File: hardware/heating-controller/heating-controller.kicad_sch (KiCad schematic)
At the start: 22 parts, among them J1 LilyGo T-Display S3, J2 Temperature_probes, J3 Power connector, K1 FINDER-32.21-x000, Q1 AO3400A, U1 H11AA1

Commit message: First PCB, needs to be checked
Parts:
- added R1, R5: 15k, Resistor_SMD:R_0603_1608Metric, symbol Device:R
- C1: renamed from C2; footprint Resistor_SMD:R_0201_0603Metric -> Capacitor_SMD:C_0603_1608Metric
- renumbered C3 to C2, C1 to C3, F2 to F1, F1 to F2, R3 to R2, R2 to R3, R1 to R4, R4 to R6, R5 to R7, R6 to R8, RV2 to RV1, RV1 to RV2
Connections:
- net EXT_TEMP_1 is gone; now on net EXT_TEMP: J2.1 (Pin_1)
- net LIM_TEMP_1 is gone; now on net LIMITER_TEMP: J2.3 (Pin_3)
- net +3.3V: now also R1.1, R5.1
- net EXT_TEMP: now also R1.2
- net LIMITER_TEMP: now also R5.2
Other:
- note added: "NTC acquisition"
- moved on the sheet: C1, C2, C3, D1, D2, F1, F2, K1, PS1, Q1, R2, R3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

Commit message: WIP
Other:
- note added: "(ADC1_CH0) 1"
- note added: "(ADC1_CH1) 2"
- note added: "(GPIO 10) 10"
- note added: "(GPIO 11) 11"
- note added: "(GPIO 12) 12"
- note added: "(GPIO 13) 13"
- note added: "(GPIO 3) 3"
- note added: "3V"
- note added: "5V"
- note added: "GND"
- note added: "NC"
- moved on the sheet: C1, C2, C3, D1, D2, F1, F2, J1, J2, J3, K1, PS1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

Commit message: WIP
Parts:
- added D1: 1N4148WS, Diode_SMD:D_SOD-323, symbol Diode:1N4148WS
- added D3: LED, LED_SMD:LED_0805_2012Metric, symbol Device:LED_Small
- added J4: EXT_LED, Connector_PinHeader_2.54mm:PinHeader_1x02_P2.54mm_Vertical, symbol Connector_Generic:Conn_01x02
- added R7, R9: 470, Resistor_SMD:R_0603_1608Metric, symbol Device:R
- C3: renamed from C2; footprint Capacitor_THT:C_Radial_D6.3mm_H7.0mm_P2.50mm -> Capacitor_THT:C_Radial_D10.0mm_H12.5mm_P5.00mm
- J1: renamed from J2; footprint Connector_Phoenix_MSTB:PhoenixContact_MSTBVA_2,5_4-G_1x04_P5.00mm_Vertical -> TerminalBlock_Phoenix:TerminalBlock_Phoenix_MKDS-3-4-5.08_1x04_P5.08mm_Horizontal
- J3: footprint Connector_Phoenix_MSTB:PhoenixContact_MSTBVA_2,5_7-G_1x07_P5.00mm_Vertical -> TerminalBlock_Phoenix:TerminalBlock_Phoenix_MKDS-3-7-5.08_1x07_P5.08mm_Horizontal
- R5: renamed from R2; footprint Resistor_THT:R_Axial_DIN0204_L3.6mm_D1.6mm_P5.08mm_Horizontal -> Resistor_THT:R_Axial_DIN0614_L14.3mm_D5.7mm_P15.24mm_Horizontal
- renumbered C3 to C1, C1 to C2, D1 to D2, D2 to D4, F2 to F1, F1 to F2, J1 to J2, R8 to R10, R3 to R2, R4 to R3, R5 to R4, R7 to R8, RV2 to RV1, RV1 to RV2
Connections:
- net +5V: now also D1.2 (A), R7.2, R9.2; no longer J2.12 (Pin_12)
- net at D4.2 (A), K1.A2, Q1.3 (D): now also D3.1 (K), J4.1 (Pin_1)
- new net: D3.2 (A), R9.1
- new net: J4.2 (Pin_2), R7.1
- new net: D1.1 (K), J2.12 (Pin_12)
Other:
- moved on the sheet: D4

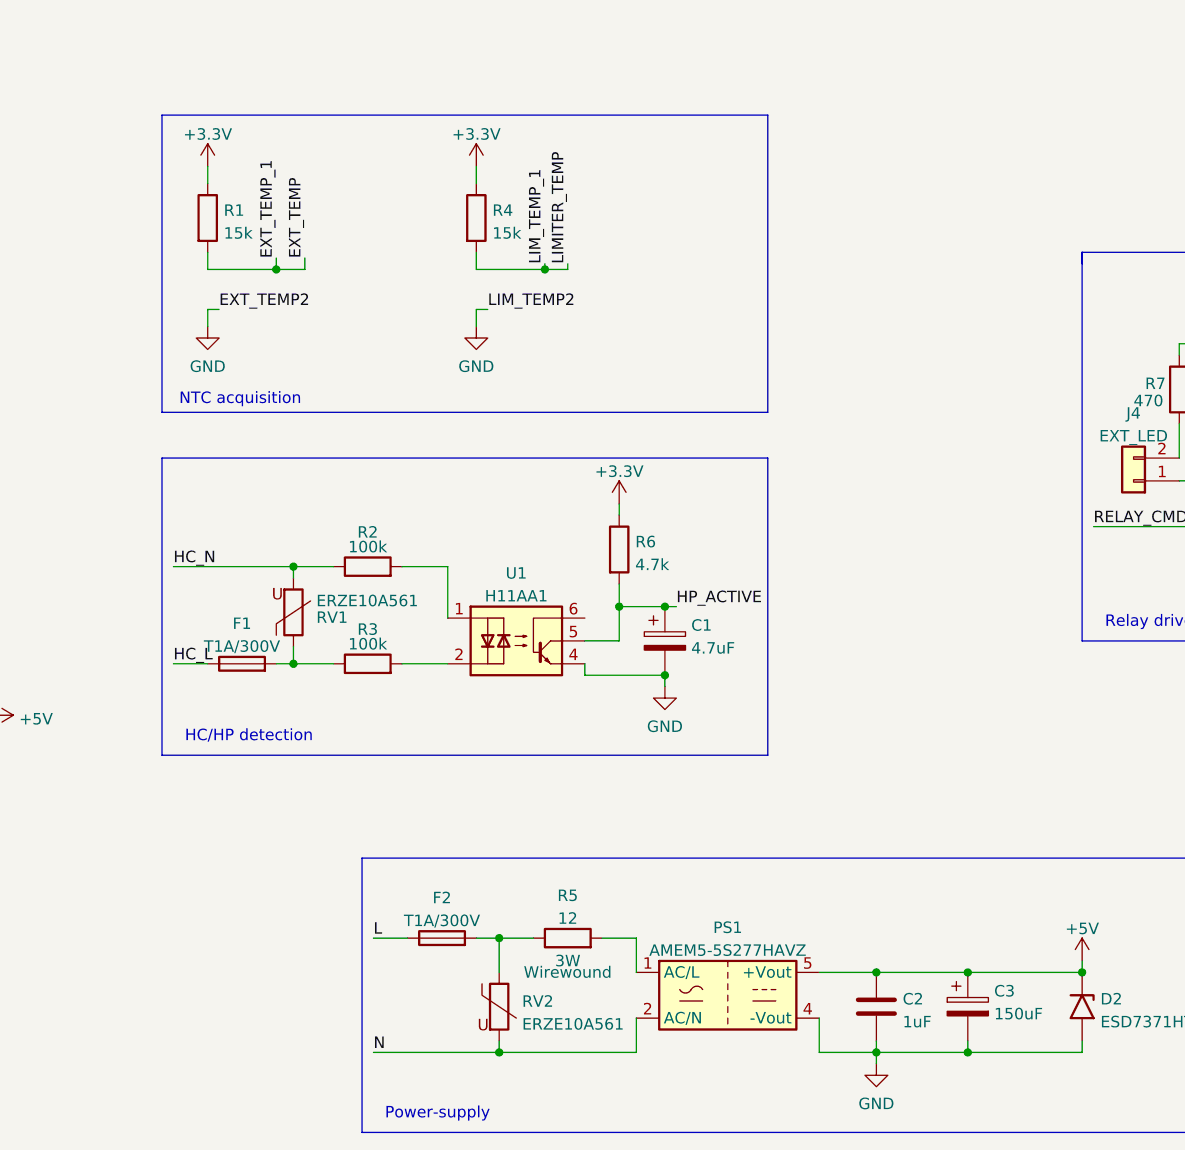
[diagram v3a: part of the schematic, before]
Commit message: Added 10uF capacitors to NTC
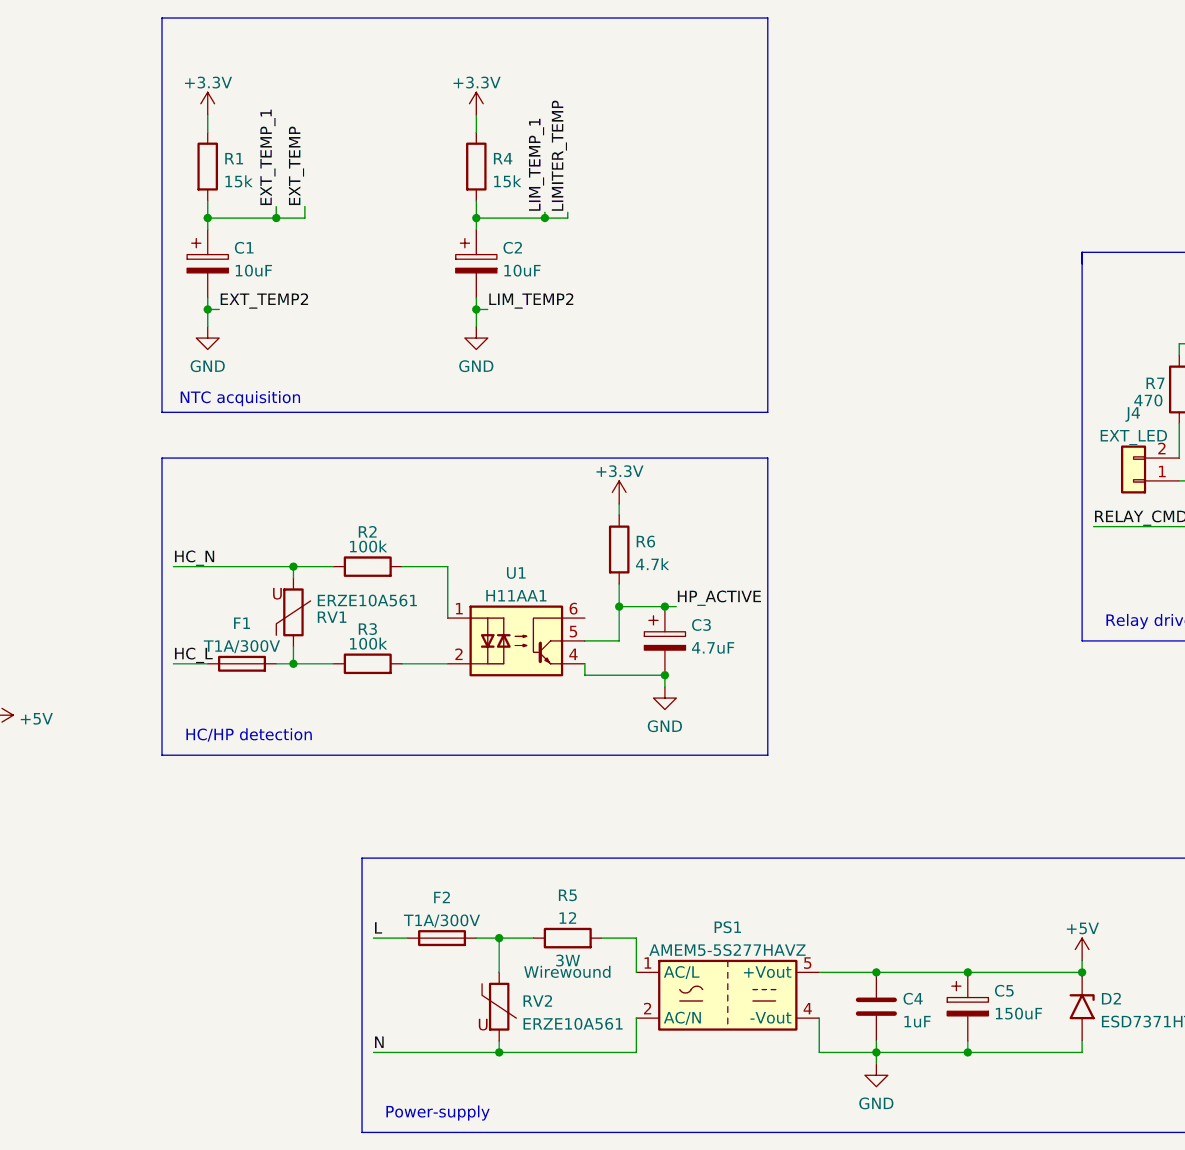
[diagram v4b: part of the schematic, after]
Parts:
- added C1, C2: 10uF, Capacitor_SMD:C_0805_2012Metric, symbol Device:C_Polarized
- renumbered C1 to C3, C2 to C4, C3 to C5
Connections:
- net EXT_TEMP: now also C1.1
- net GND: now also C1.2, C2.2
- net LIMITER_TEMP: now also C2.1
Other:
- moved on the sheet: R1, R4

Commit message: WIP
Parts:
- added J5: USER_LED, Connector_PinHeader_2.54mm:PinHeader_1x02_P2.54mm_Vertical, symbol Connector_Generic:Conn_01x02
- added Q1: AO3400A, Package_TO_SOT_SMD:SOT-23, symbol Transistor_FET:AO3400A
- added R11: 100k, Resistor_SMD:R_0603_1608Metric, symbol Device:R
- added R13: 470, Resistor_SMD:R_0603_1608Metric, symbol Device:R
- added R8: 1k, Resistor_SMD:R_0603_1608Metric, symbol Device:R
- R10: renamed from R9; value 470 -> 2k
- renumbered D3 to D2, D2 to D3, Q1 to Q2, R10 to R12, R8 to R9
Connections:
- net EXT_TEMP_2 is gone; now on net GND: J1.2 (Pin_2)
- net LIM_TEMP_2 is gone; now on net GND: J1.4 (Pin_4)
- net +5V: now also R13.2
- net GND: now also Q1.2 (S), R11.2
- net USER_LED: now reaches J2.6 (Pin_6)
- net USER_LED: now also R8.1
- new net: Q1.1 (G), R11.1, R8.2
- new net: J5.1 (Pin_1), Q1.3 (D)
- new net: J5.2 (Pin_2), R13.1
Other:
- note added: "User LED"
- moved on the sheet: D2, D4, J4, K1, Q2, R10, R12, R7, R9

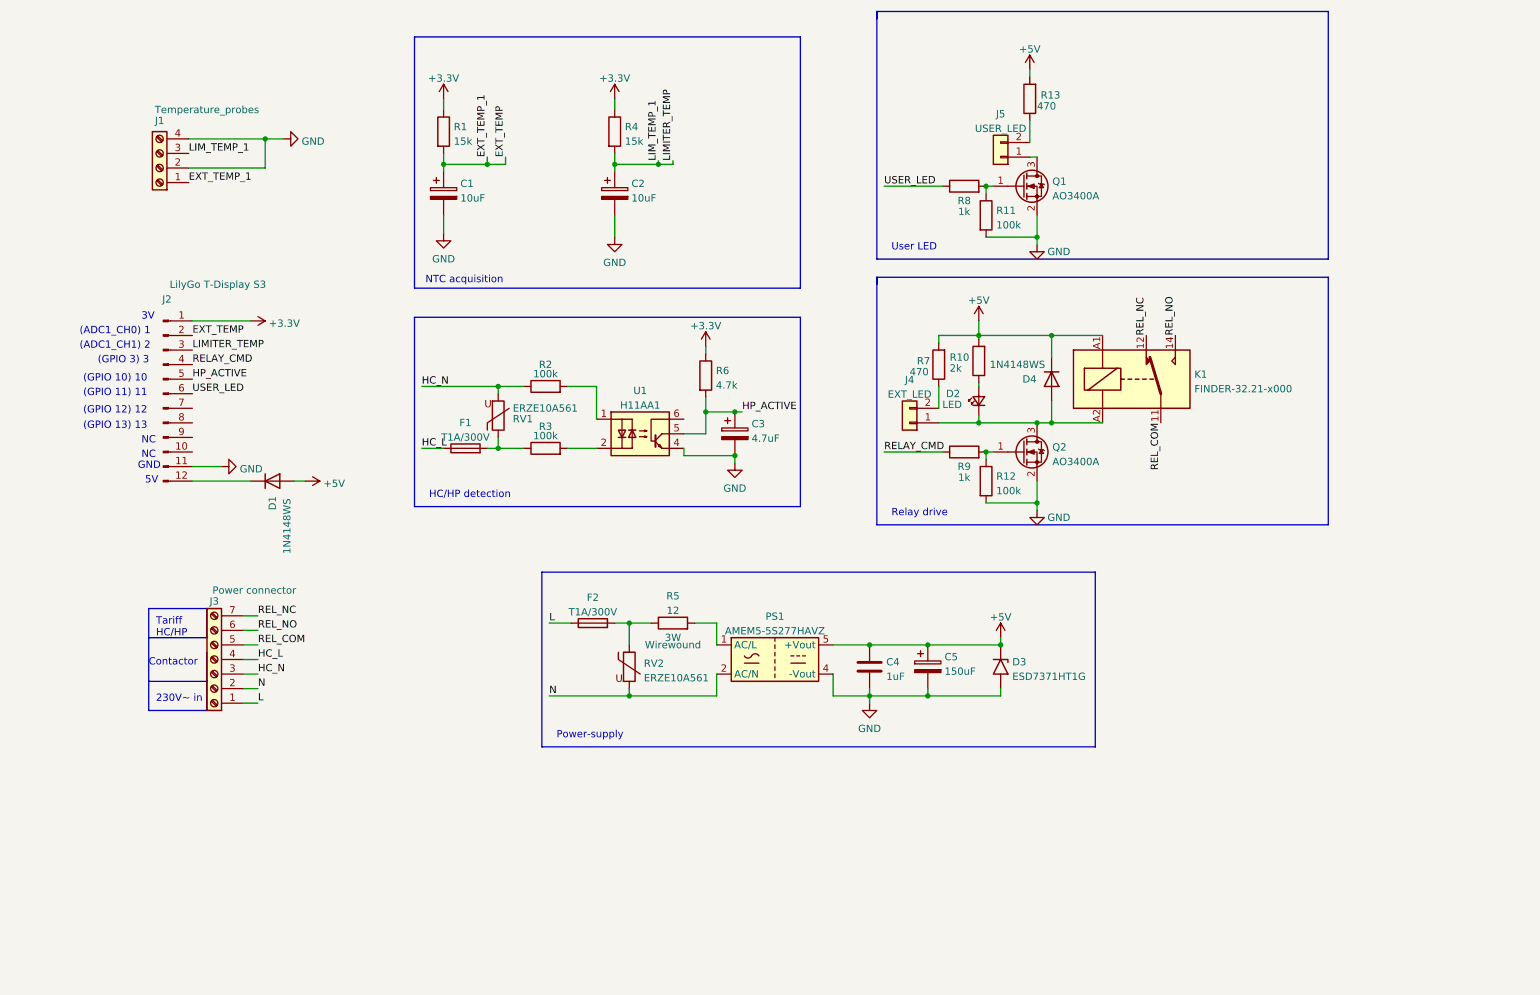
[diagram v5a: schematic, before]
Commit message: Migrated to KiCad 7 and remove custom AC/DC
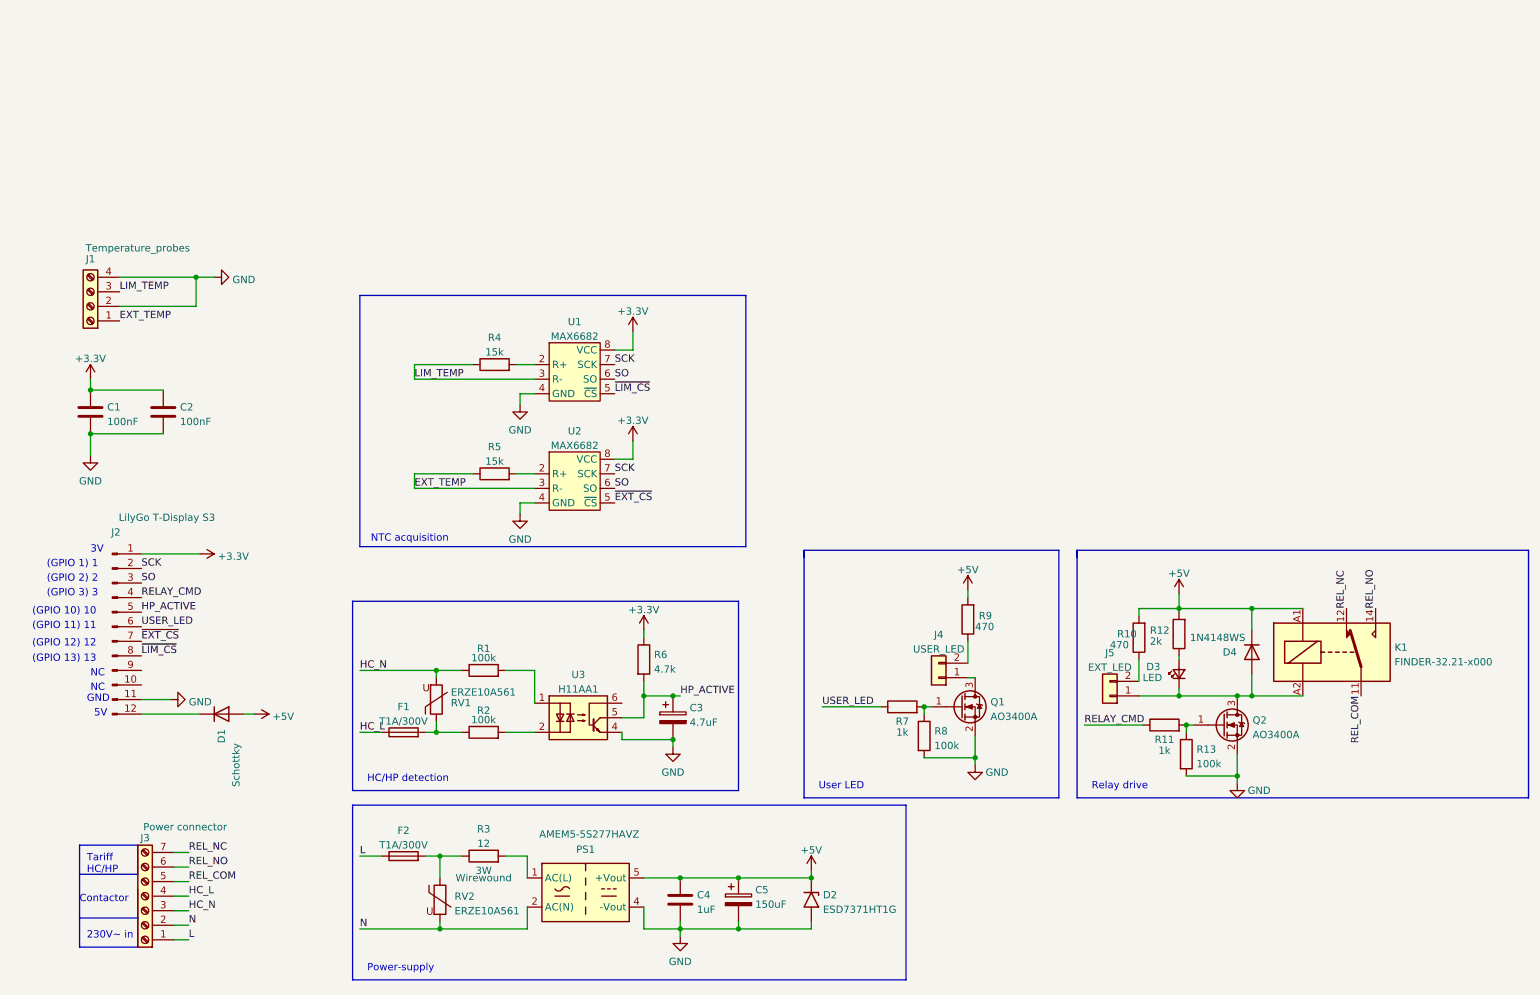
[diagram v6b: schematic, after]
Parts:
- removed C1, C2: 10uF, Capacitor_SMD:C_0805_2012Metric, symbol Device:C_Polarized
- removed R4: 15k, Resistor_SMD:R_0603_1608Metric, symbol Device:R
- added C1, C2: 100nF, Capacitor_SMD:C_0603_1608Metric_Pad1.08x0.95mm_HandSolder, symbol Device:C
- added R5: 15k, Resistor_SMD:R_0603_1608Metric, symbol Device:R
- added U1, U2: MAX6682, Package_SO:MSOP-8_3x3mm_P0.65mm, symbol heating-controller:MAX6682
- D1: value 1N4148WS -> Schottky; footprint Diode_SMD:D_SOD-323 -> Diode_SMD:D_SOD-123
- PS1: footprint heating-controller:Converter_ACDC_aimtec_AMEM5 -> Converter_ACDC:Converter_ACDC_Murata_BAC05SxxDC_THT; symbol heating-controller:AMEM5-5S277HAVZ -> Converter_ACDC:RAC05-05SK
- renumbered D3 to D2, D2 to D3, J5 to J4, J4 to J5, R2 to R1, R7 to R10, R9 to R11, R10 to R12, R12 to R13, R3 to R2, R5 to R3, R1 to R4, R8 to R7, R11 to R8, R13 to R9, U1 to U3
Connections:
- net +3.3V: now also C1.1, C2.1, U1.8 (VCC), U2.8 (VCC); no longer R4.1
- net EXT_TEMP: now also R5.1, U2.3 (R-); no longer J2.2 (Pin_2), R4.2
- net GND: now also C1.2, C2.2, U1.4 (GND), U2.4 (GND)
- net ~{EXT_CS}: now reaches J2.7 (Pin_7)
- net ~{EXT_CS}: now also U2.5 (~{CS})
- net ~{LIM_CS}: now reaches J2.8 (Pin_8)
- net ~{LIM_CS}: now also U1.5 (~{CS})
- net LIMITER_TEMP renamed LIM_TEMP
- net LIM_TEMP: now also R4.1, U1.3 (R-); no longer J2.3 (Pin_3)
- new net: R5.2, U2.2 (R+)
- new net: R4.2, U1.2 (R+)
- new net SCK: J2.2 (Pin_2), U1.7 (SCK), U2.7 (SCK)
- new net SO: J2.3 (Pin_3), U1.6 (SO), U2.6 (SO)
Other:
- note added: "(GPIO 1) 1"
- note added: "(GPIO 2) 2"
- note removed: "(ADC1_CH0) 1"
- note removed: "(ADC1_CH1) 2"
- moved on the sheet: C3, C4, C5, D1, D2, D3, D4, F1, F2, J1, J2, J3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
